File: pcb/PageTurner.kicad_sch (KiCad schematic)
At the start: 19 parts, among them J1 AudioJack2, J2 AudioJack2, J3 USB_C_Receptacle, J5 TC2030_SWD, SW1 RST, SW2 BOOT, U1 STM32F042F6Px, U2 TPS7A0533PDBV

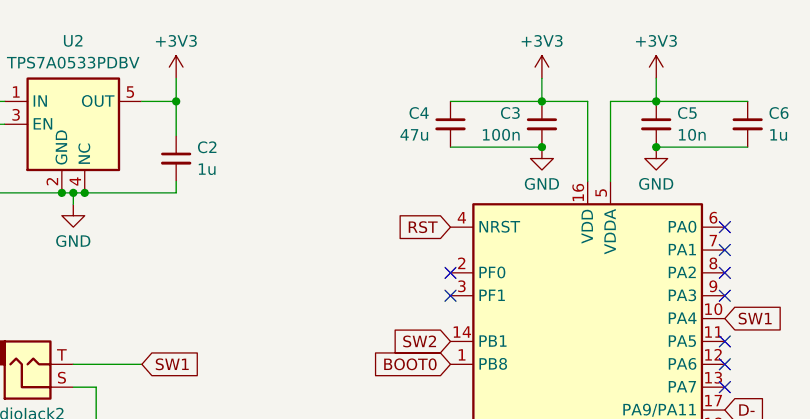
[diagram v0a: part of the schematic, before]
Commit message: Update bom, fix decoupling capacitor value
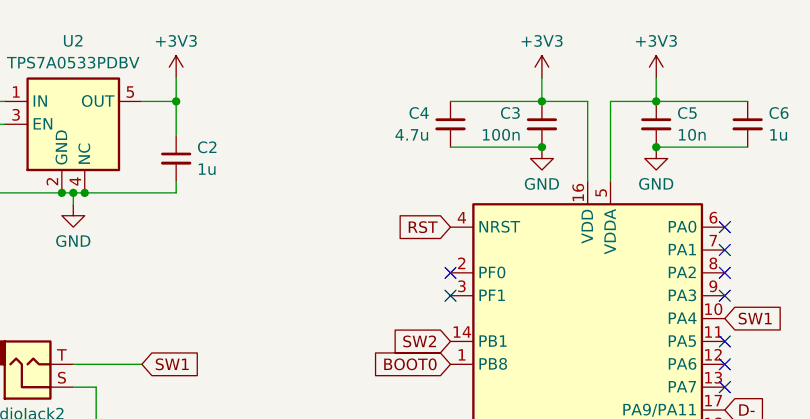
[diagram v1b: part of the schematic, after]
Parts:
- C1, C2, C3, C5, C6, C7, R1, R2, R3: Package (none) -> 0603
- C4: value 47u -> 4.7u; Package (none) -> 0603
- U1: Package (none) -> TSSOP-20
- U2: Package (none) -> SOT-23-5
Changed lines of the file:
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@@
+			)
+		)
+		(property "Package" ""
+			(at 137.16 95.25 0)
+			(effects
+				(font
+					(size 1.27 1.27)
+				)
+				(hide yes)
 			)
 		)
@@
 			)
 		)
+		(property "Package" "0603"
+			(at 217.17 54.61 0)
+			(effects
+				(font
+					(size 1.27 1.27)
+				)
+				(hide yes)
+			)
+		)
 		(pin "1"
 		)
@@
 			)
 		)
-		(property "Value" "47u"
+		(property "Value" "4.7u"
 			(at 181.8259 55.8284 0)
 			(effects
@@
 			)
 		)
+		(property "Package" "0603"
+			(at 184.15 54.61 0)
+			(effects
+				(font
+					(size 1.27 1.27)
+				)
+				(hide yes)
+			)
+		)
 		(pin "1"
 		)
@@
 		)
 		(property "Manufacturer" ""
+			(at 194.31 54.61 0)
+			(effects
+				(font
+					(size 1.27 1.27)
+				)
+				(hide yes)
+			)
+		)
+		(property "Package" "0603"
 			(at 194.31 54.61 0)
 			(effects
@@
 			)
 		)
+		(property "Package" "0603"
+			(at 163.83 143.51 0)
+			(effects
+				(font
+					(size 1.27 1.27)
+				)
+				(hide yes)
+			)
+		)
 		(pin "1"
 		)
@@
 			)
 		)
+		(property "Package" "TSSOP-20"
+			(at 199.39 81.28 0)
+			(effects
+				(font
+					(size 1.27 1.27)
+				)
+				(hide yes)
+			)
+		)
 		(pin "13"
 		)
@@
 			)
 		)
+		(property "Package" "SOT-23-5"
+			(at 142.24 54.61 0)
+			(effects
+				(font
+					(size 1.27 1.27)
+				)
+				(hide yes)
+			)
+		)
 		(pin "3"
 		)
@@
 			)
 		)
+		(property "Package" "0603"
+			(at 110.49 55.88 0)
+			(effects
+				(font
+					(size 1.27 1.27)
+				)
+				(hide yes)
+			)
+		)
 		(pin "2"
 		)
@@
 		)
 		(property "Manufacturer" ""
+			(at 130.81 58.42 0)
+			(effects
+				(font
+					(size 1.27 1.27)
+				)
+				(hide yes)
+			)
+		)
+		(property "Package" "0603"
 			(at 130.81 58.42 0)
 			(effects
@@
 			)
 		)
+		(property "Package" ""
+			(at 137.16 81.28 0)
+			(effects
+				(font
+					(size 1.27 1.27)
+				)
+				(hide yes)
+			)
+		)
 		(pin "S"
 		)
@@
 			)
 		)
+		(property "Package" ""
+			(at 137.16 142.24 0)
+			(effects
+				(font
+					(size 1.27 1.27)
+				)
+				(hide yes)
+			)
+		)
 		(pin "1"
 		)
@@
 			)
 		)
+		(property "Package" ""
+			(at 88.9 142.24 0)
+			(effects
+				(font
+					(size 1.27 1.27)
+				)
+				(hide yes)
+			)
+		)
 		(pin "3"
 		)
@@
 			)
 		)
+		(property "Package" "0603"
+			(at 153.67 58.42 0)
+			(effects
+				(font
+					(size 1.27 1.27)
+				)
+				(hide yes)
+			)
+		)
 		(pin "1"
 		)
@@
 			)
 		)
+		(property "Package" ""
+			(at 85.09 76.2 0)
+			(effects
+				(font
+					(size 1.27 1.27)
+				)
+				(hide yes)
+			)
+		)
 		(pin "A6"
 		)
@@
 			)
 		)
+		(property "Package" ""
+			(at 168.91 139.7 0)
+			(effects
+				(font
+					(size 1.27 1.27)
+				)
+				(hide yes)
+			)
+		)
 		(pin "1"
 		)
@@
 			)
 		)
+		(property "Package" "0603"
+			(at 110.49 58.42 0)
+			(effects
+				(font
+					(size 1.27 1.27)
+				)
+				(hide yes)
+			)
+		)
 		(pin "2"
 		)
@@
 			)
 		)
+		(property "Package" "0603"
+			(at 203.2 146.05 0)
+			(effects
+				(font
+					(size 1.27 1.27)
+				)
+				(hide yes)
+			)
+		)
 		(pin "2"
 		)
@@
 			)
 		)
+		(property "Package" ""
+			(at 203.2 135.89 0)
+			(effects
+				(font
+					(size 1.27 1.27)
+				)
+				(hide yes)
+			)
+		)
 		(pin "1"
 		)
@@
 			(at 207.01 54.61 0)
 			(effects
+				(font
+					(size 1.27 1.27)
+				)
+				(hide yes)
+			)
+		)
+		(property "Package" "0603"
+			(at 207.01 54.61 0)
+			(effects

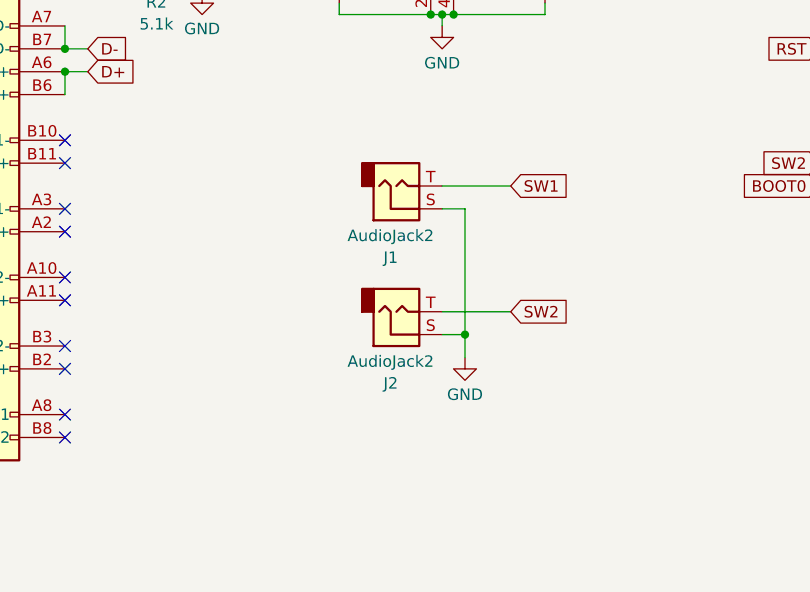
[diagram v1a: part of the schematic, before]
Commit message: Add ESD diodes for pedal inputs
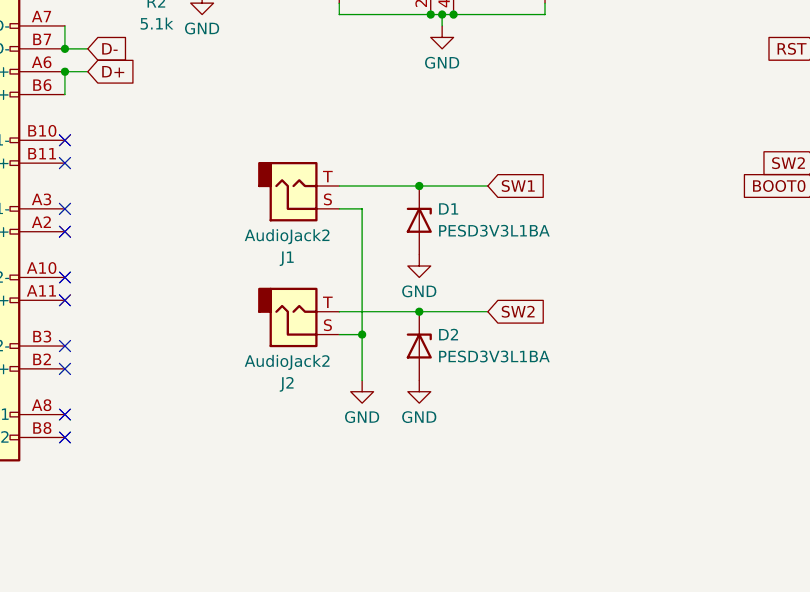
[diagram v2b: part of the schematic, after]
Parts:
- added D1, D2: PESD3V3L1BA, Diode_SMD:D_SOD-323_HandSoldering, symbol Device:D_Zener
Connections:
- net GND: now also D1.2 (A), D2.2 (A)
- net SW1: now also D1.1 (K)
- net SW2: now also D2.1 (K)
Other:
- moved on the sheet: J1, J2

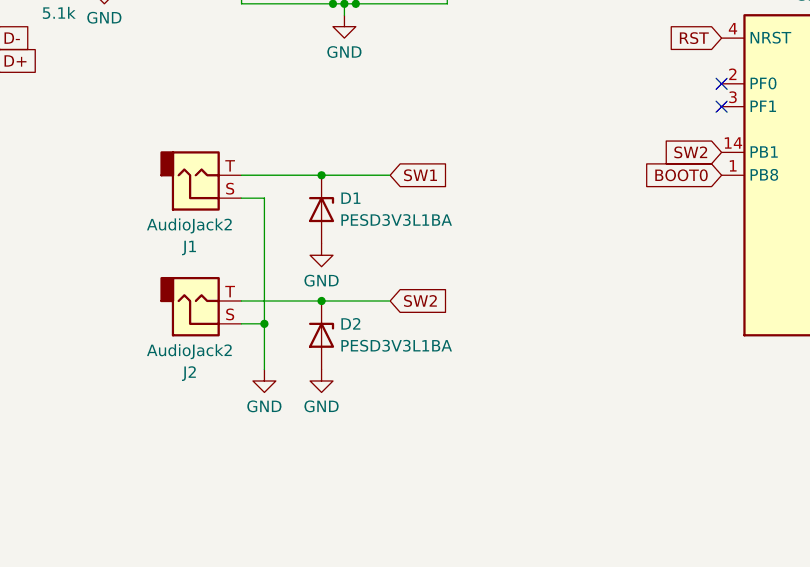
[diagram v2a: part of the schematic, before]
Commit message: Use cheaper ESD diode
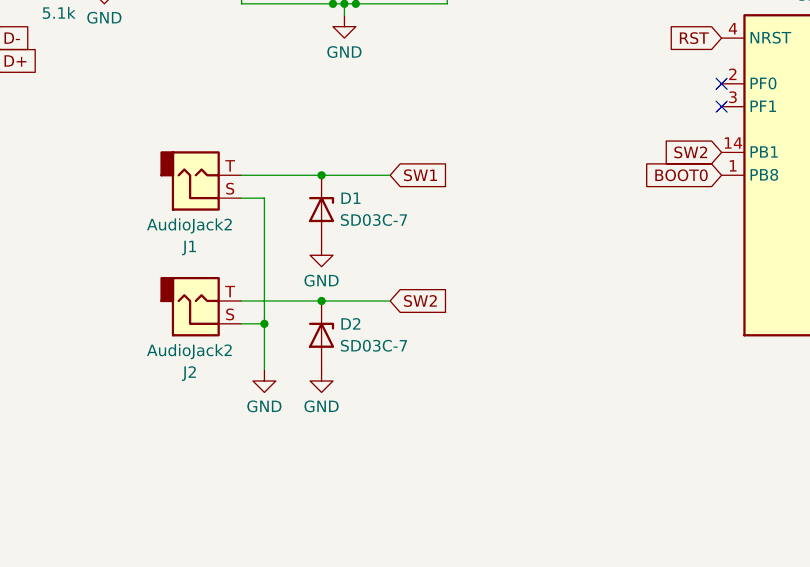
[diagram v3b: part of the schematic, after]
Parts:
- D1, D2: value PESD3V3L1BA -> SD03C-7
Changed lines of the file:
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@@
 			)
 		)
-		(property "Value" "PESD3V3L1BA"
+		(property "Value" "SD03C-7"
 			(at 141.732 86.3021 90)
 			(effects
@@
 			)
 		)
-		(property "Datasheet" "~"
+		(property "Datasheet" "https://www.diodes.com/assets/Datasheets/SD03C.pdf"
 			(at 139.7 85.09 0)
 			(effects
@@
 			)
 		)
-		(property "Value" "PESD3V3L1BA"
+		(property "Value" "SD03C-7"
 			(at 141.732 100.2721 90)
 			(effects
@@
 			)
 		)
-		(property "Datasheet" "~"
+		(property "Datasheet" "https://www.diodes.com/assets/Datasheets/SD03C.pdf"
 			(at 139.7 99.06 0)
 			(effects

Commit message: Switch to a cheaper and smaller USB connector
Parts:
- J3: footprint PageTurner:USB_C_Receptacle_JAE_DX07S024WJ3R400 -> PageTurner:USB_C_Receptacle_GCT_USB_4145
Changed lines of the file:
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@@
 			)
 		)
-		(property "Footprint" "PageTurner:USB_C_Receptacle_JAE_DX07S024WJ3R400"
+		(property "Footprint" "PageTurner:USB_C_Receptacle_GCT_USB_4145"
 			(at 88.9 76.2 0)
 			(effects

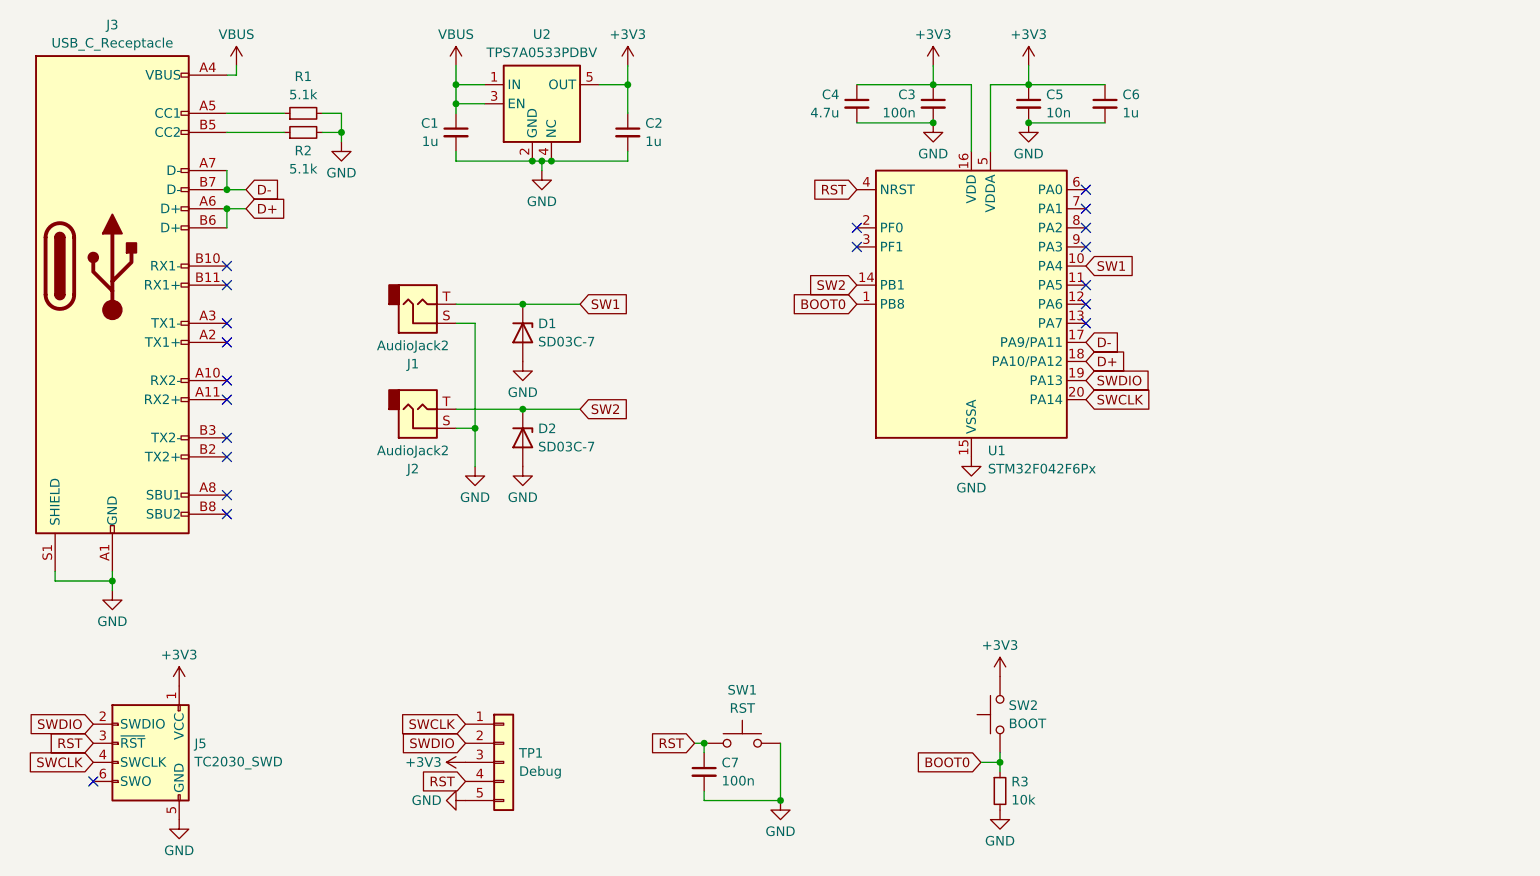
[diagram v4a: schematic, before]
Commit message: Switch to 4 layers, add USB ESD diode
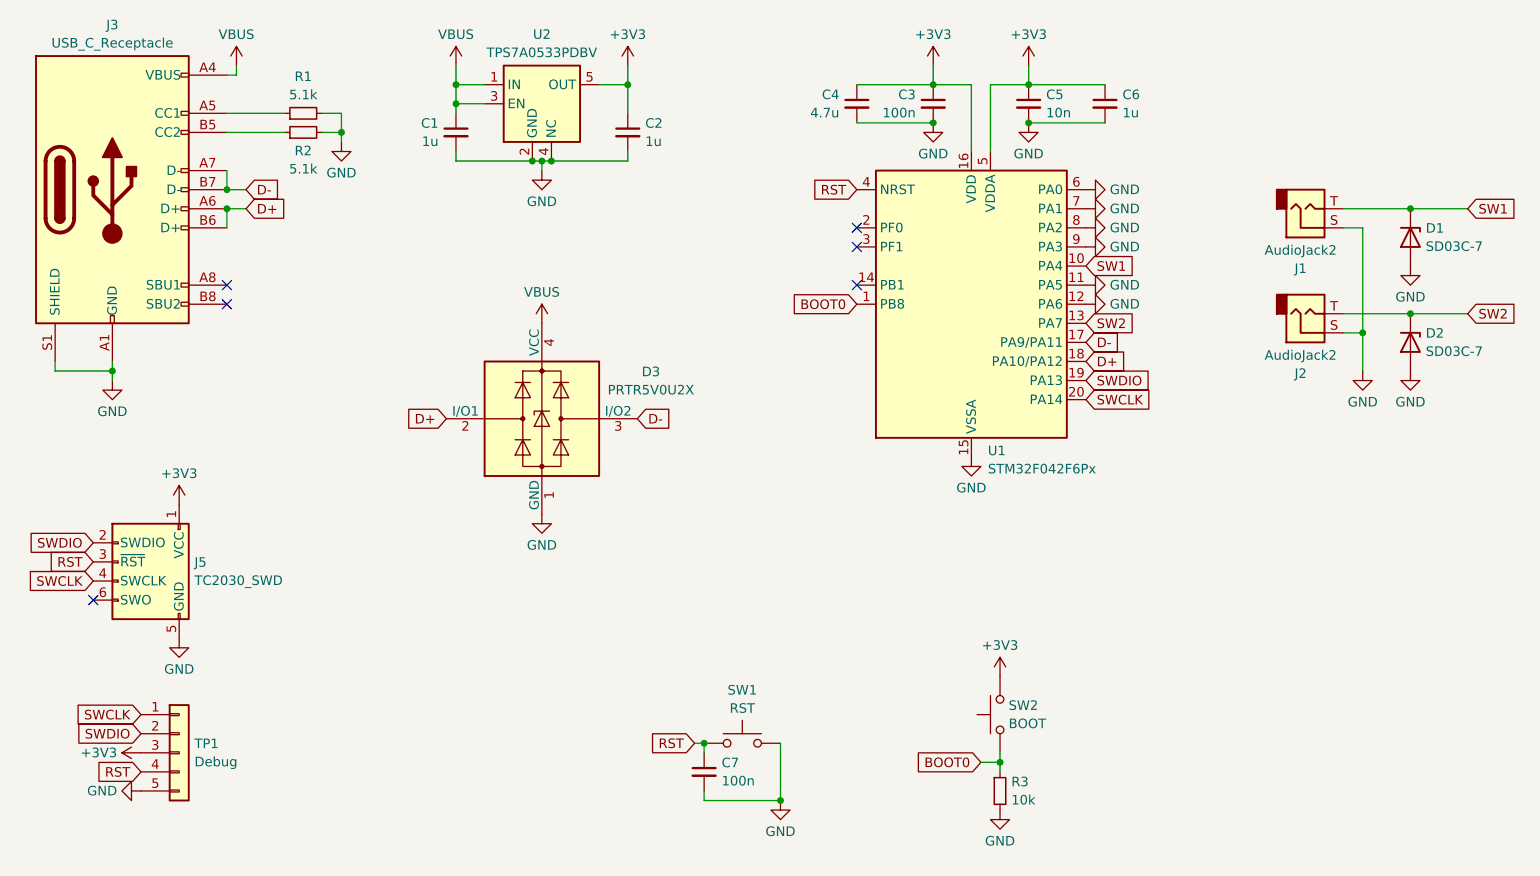
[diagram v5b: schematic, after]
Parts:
- added D3: PRTR5V0U2X, Package_TO_SOT_SMD:SOT-143, symbol Power_Protection:PRTR5V0U2X
- J3: symbol Connector:USB_C_Receptacle -> Connector:USB_C_Receptacle_USB2.0_16P
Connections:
- net D+: now also D3.2 (I/O1)
- net D-: now also D3.3 (I/O2)
- net GND: now also U1.11 (PA5), U1.12 (PA6), U1.6 (PA0), U1.7 (PA1), U1.8 (PA2), U1.9 (PA3), D3.1 (GND)
- net SW2: now also U1.13 (PA7); no longer U1.14 (PB1)
- net VBUS: now also D3.4 (VCC)
- no-connect marks 20 -> 6
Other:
- moved on the sheet: D1, D2, J1, J2, J5, TP1

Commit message: General cleanup
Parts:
- D1, D2: Manufacturer (none) -> Diodes Incorporated; Manufacturer Part Number (none) -> SD03C-7
- D3: Manufacturer (none) -> Nexperia; Manufacturer Part Number (none) -> PRTR5V0U2X,215
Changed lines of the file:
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@@
+			)
+		)
+		(property "Manufacturer" "Diodes Incorporated"
+			(at 257.81 72.39 0)
+			(effects
+				(font
+					(size 1.27 1.27)
+				)
+				(hide yes)
+			)
+		)
+		(property "Manufacturer Part Number" "SD03C-7"
+			(at 257.81 72.39 0)
+			(effects
+				(font
+					(size 1.27 1.27)
+				)
+				(hide yes)
 			)
 		)
@@
 			)
 		)
+		(property "Manufacturer" "Nexperia"
+			(at 142.24 96.52 0)
+			(effects
+				(font
+					(size 1.27 1.27)
+				)
+				(hide yes)
+			)
+		)
+		(property "Manufacturer Part Number" "PRTR5V0U2X,215"
+			(at 142.24 96.52 0)
+			(effects
+				(font
+					(size 1.27 1.27)
+				)
+				(hide yes)
+			)
+		)
 		(pin "2"
 		)
@@
 			(at 257.81 86.36 0)
 			(effects
+				(font
+					(size 1.27 1.27)
+				)
+				(hide yes)
+			)
+		)
+		(property "Manufacturer" "Diodes Incorporated"
+			(at 257.81 86.36 0)
+			(effects
+				(font
+					(size 1.27 1.27)
+				)
+				(hide yes)
+			)
+		)
+		(property "Manufacturer Part Number" "SD03C-7"
+			(at 257.81 86.36 0)
+			(effects
